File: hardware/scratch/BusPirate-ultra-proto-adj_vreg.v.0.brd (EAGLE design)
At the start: 45.4 x 29.2 mm, 18 parts, among them J1 CON_HEADER_1X02-PTH, J2 CON_HEADER_1X02-PTH, J3 CON_HEADER_1X02-PTH, Q1 DMMT3906W, Q3 FDS6575, U1 LM317T, U2 MCP6001

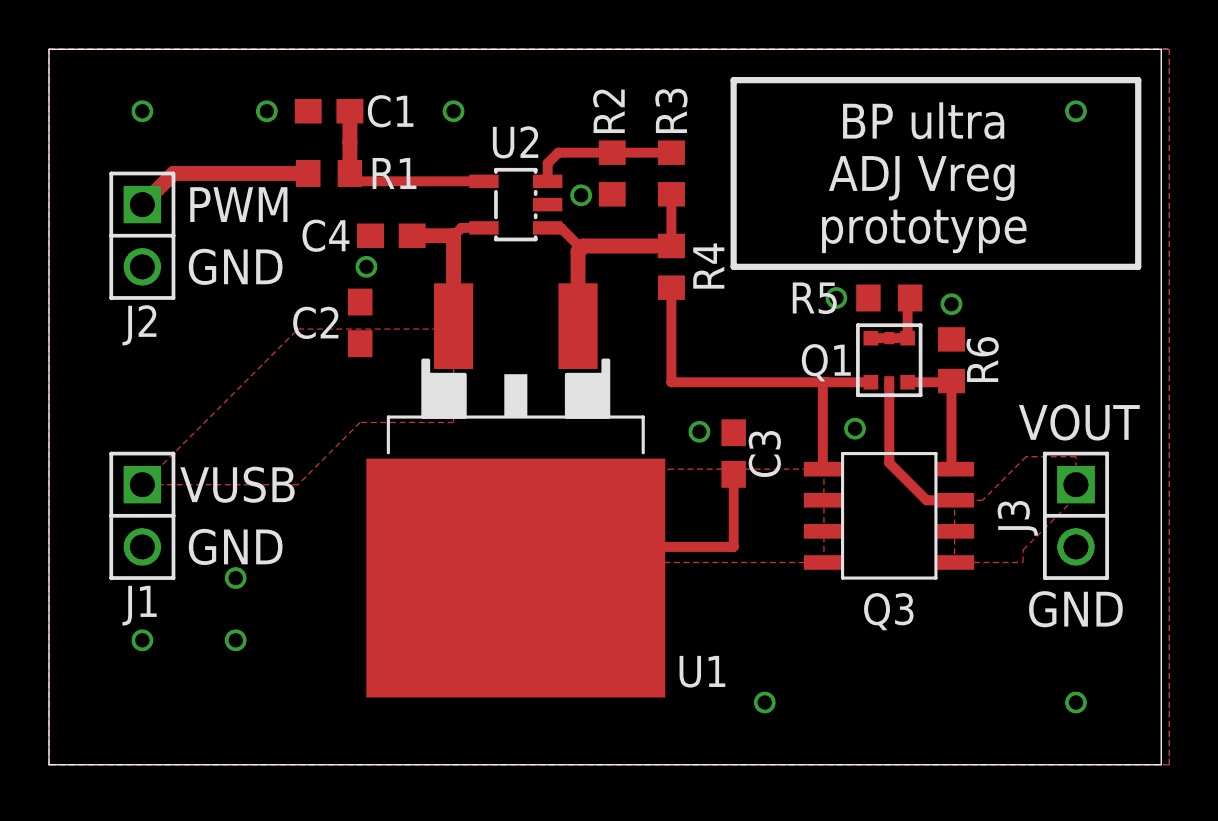
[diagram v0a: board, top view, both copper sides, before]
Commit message: changed vreg and pass mosfet
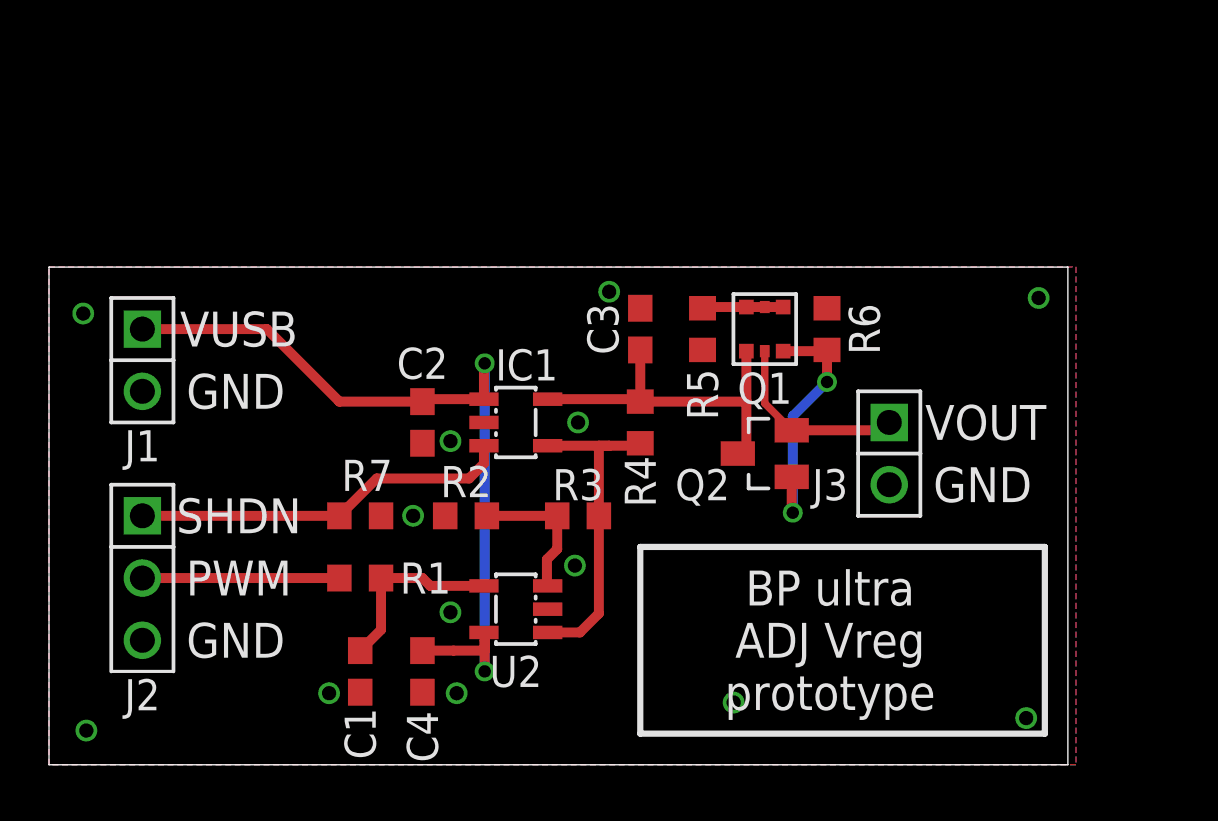
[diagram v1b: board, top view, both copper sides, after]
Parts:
- removed Q3: FDS6575, dp_devices.v6:SO-8
- removed U1: LM317T, dp_devices.v6:D2PAK
- added IC1: MCP1824_ADJ, dp_devices.v6:SOT-23-5
- added Q2: (no value), dp_devices.v6:SOT-23
- added R7: 10K, dp_devices.v6:R603
- J2: value CON_HEADER_1X02-PTH -> CON_HEADER_1X03-PTH; device dp_devices.v6:M1X2 -> dp_devices.v6:M1X3
- moved C1 22.9 mm to (12.7, 3.81), turned to 270 degrees
- moved C4 17.8 mm to (15.2, 3.81), turned to 270 degrees
- moved R1 16.6 mm to (12.7, 7.62)
- moved U2 16.5 mm to (19.1, 6.35)
- moved R2 15.2 mm to (17.0, 10.2), turned to 180 degrees
- moved R3 14.5 mm to (21.6, 10.2), turned to 180 degrees
- moved J2 11.4 mm to (3.81, 10.2)
- moved J3 8.03 mm to (34.3, 12.7)
- moved R5 7.73 mm to (26.7, 17.8), turned to 90 degrees
- moved R4 6.48 mm to (24.1, 14.0), turned to 90 degrees
- moved C3 6.35 mm to (24.1, 17.8)
- moved J1 6.35 mm to (3.81, 16.5)
- moved Q1 5.24 mm to (29.2, 17.8)
- moved R6 5.24 mm to (31.8, 17.8)
- moved C2 4.79 mm to (15.2, 14.0), turned to 270 degrees
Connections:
- new net !SHDN: IC1.3, J2.1, R7.1
- net GND: now also IC1.2, J2.3, R7.2; no longer J2.2
- net N$1: now also IC1.5, Q2.3; no longer Q3.5, Q3.6, Q3.7, Q3.8, U1.2
- net N$4: now also Q2.1; no longer Q3.4
- net N$8: now also IC1.4; no longer U1.1
- net PWM: now also J2.2; no longer J2.1
- net VPU: now also Q2.2; no longer Q3.1, Q3.2, Q3.3
- net VUSB: now also IC1.1; no longer U1.3
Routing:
- net VUSB: track 6.75 -> 33.8 mm, vias 0 -> 2
- net !SHDN: track 0.00 -> 15.6 mm
- net N$1: track 28.1 -> 14.7 mm
- net N$4: track 5.47 -> 10.5 mm, vias 0 -> 2
- net N$8: track 10.8 -> 13.5 mm
- net VPU: track 6.61 -> 7.80 mm
- net PWM: track 7.30 -> 8.04 mm
- removed copper zone on layer 1, net N$1
- removed copper zone on layer 1, net VPU
- removed copper zone on layer 1, net VUSB
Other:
- board size 45.4 x 29.2 mm -> 41.6 x 20.3 mm
- board text added: "SHDN"
